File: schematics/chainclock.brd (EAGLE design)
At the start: 55 x 46.5 mm, 21 parts, among them SW1 ROTARTY_ENCODER

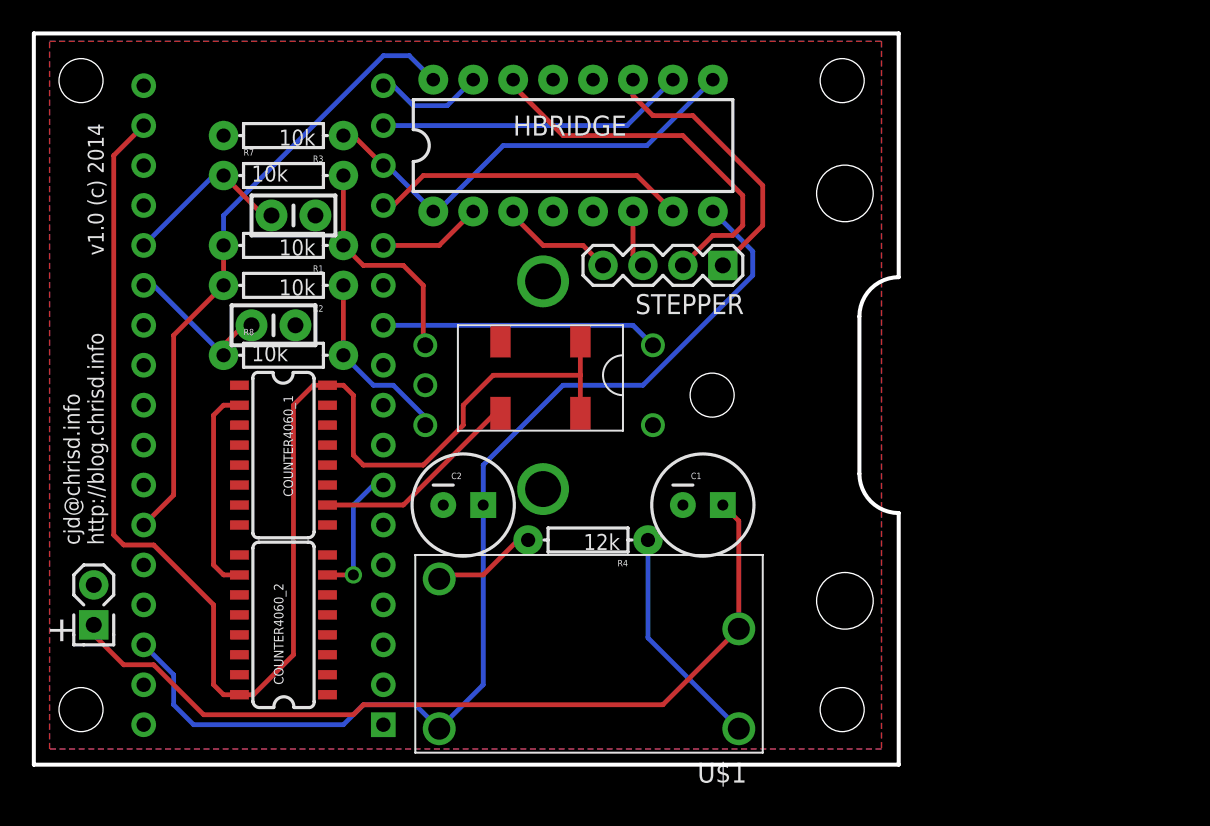
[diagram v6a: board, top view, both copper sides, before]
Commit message: Move power header
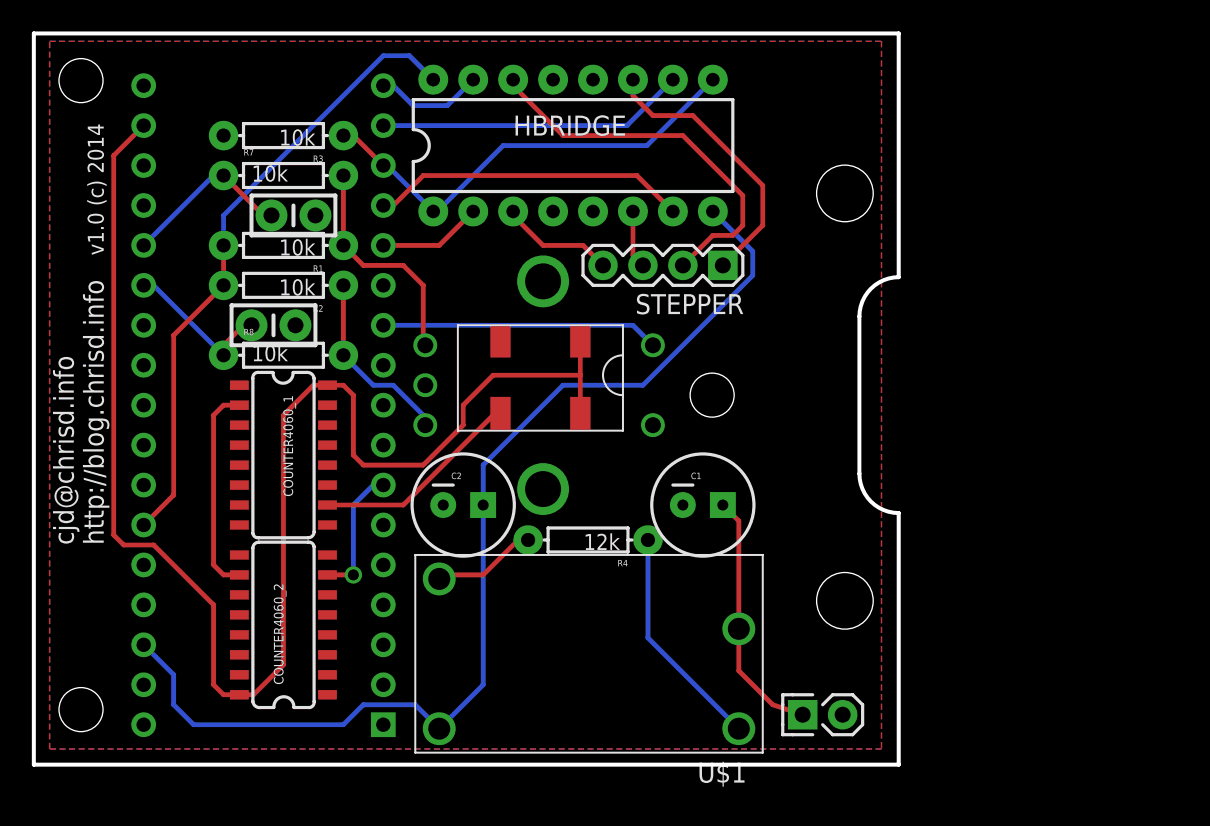
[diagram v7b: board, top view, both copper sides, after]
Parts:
- moved JP1 45.4 mm to (48.9, 3.17), turned to 0 degrees
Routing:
- net VBATT: track 54.3 -> 16.0 mm
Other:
- board text removed: "+"
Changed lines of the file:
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@@
 <hole x="3" y="43.5" drill="2.8"/>
 <hole x="43.135" y="23.5" drill="2.8"/>
-<text x="4.445" y="13.97" size="1.016" layer="21" rot="R90">cjd@chrisd.info
+<text x="4.445" y="13.97" size="1.27" layer="21" rot="R90">cjd@chrisd.info
 http://blog.chrisd.info</text>
-<hole x="51.405" y="3.5" drill="2.8"/>
-<hole x="51.405" y="43.5" drill="2.8"/>
 <wire x1="0" y1="0" x2="0" y2="46.5" width="0.254" layer="20"/>
 <wire x1="0" y1="46.5" x2="55" y2="46.5" width="0.254" layer="20"/>
@@
 <wire x1="55" y1="0" x2="0" y2="0" width="0.254" layer="20"/>
 <text x="4.445" y="32.385" size="1.016" layer="21" rot="R90">v1.0 (c) 2014</text>
-<text x="2.54" y="7.62" size="1.778" layer="21" rot="R90">+</text>
 </plain>
 <attributes>
@@
 <element name="C2" library="SparkFun-Capacitors" package="CPOL-RADIAL-100UF-25V" value="" x="27.305" y="16.51"/>
 <element name="R4" library="SparkFun-Resistors" package="AXIAL-0.3EZ" value="12k" x="35.2425" y="14.2875" rot="R180"/>
-<element name="JP1" library="desjardins" package="MOLEX-1X2" value="M02POLAR" x="3.81" y="8.89" rot="R90"/>
+<element name="JP1" library="desjardins" package="MOLEX-1X2" value="M02POLAR" x="48.895" y="3.175"/>
 <element name="COUNTER4060_1" library="desjardins" package="SO016" value="4060SOIC16" x="15.875" y="19.685" rot="R270"/>
 <element name="COUNTER4060_2" library="desjardins" package="SO016" value="4060SOIC16" x="15.875" y="8.89" rot="R90"/>
@@
 <wire x1="12.065" y1="4.445" x2="13.075" y2="4.445" width="0.3048" layer="1"/>
 <wire x1="18.675" y1="24.13" x2="17.78" y2="24.13" width="0.3048" layer="1"/>
-<wire x1="17.78" y1="24.13" x2="16.51" y2="22.86" width="0.3048" layer="1"/>
-<wire x1="16.51" y1="22.86" x2="16.51" y2="6.985" width="0.3048" layer="1"/>
-<wire x1="16.51" y1="6.985" x2="13.97" y2="4.445" width="0.3048" layer="1"/>
+<wire x1="17.78" y1="24.13" x2="15.875" y2="22.225" width="0.3048" layer="1"/>
+<wire x1="15.875" y1="22.225" x2="15.875" y2="6.35" width="0.3048" layer="1"/>
+<wire x1="15.875" y1="6.35" x2="13.97" y2="4.445" width="0.3048" layer="1"/>
 <wire x1="13.97" y1="4.445" x2="13.075" y2="4.445" width="0.3048" layer="1"/>
 </signal>
@@
 <contactref element="C1" pad="1"/>
 <contactref element="JP1" pad="1"/>
-<wire x1="3.81" y1="8.89" x2="3.81" y2="8.255" width="0.3048" layer="1"/>
-<wire x1="3.81" y1="8.255" x2="5.715" y2="6.35" width="0.3048" layer="1"/>
-<wire x1="5.715" y1="6.35" x2="7.62" y2="6.35" width="0.3048" layer="1"/>
-<wire x1="7.62" y1="6.35" x2="10.795" y2="3.175" width="0.3048" layer="1"/>
-<wire x1="10.795" y1="3.175" x2="20.32" y2="3.175" width="0.3048" layer="1"/>
-<wire x1="20.32" y1="3.175" x2="20.955" y2="3.81" width="0.3048" layer="1"/>
-<wire x1="20.955" y1="3.81" x2="40.005" y2="3.81" width="0.3048" layer="1"/>
-<wire x1="40.005" y1="3.81" x2="44.831" y2="8.636" width="0.3048" layer="1"/>
 <wire x1="44.831" y1="8.636" x2="44.831" y2="15.494" width="0.3048" layer="1"/>
 <wire x1="44.831" y1="15.494" x2="43.815" y2="16.51" width="0.3048" layer="1"/>
+<wire x1="44.831" y1="8.636" x2="44.831" y2="5.969" width="0.3048" layer="1"/>
+<wire x1="44.831" y1="5.969" x2="46.99" y2="3.81" width="0.3048" layer="1"/>
+<wire x1="46.99" y1="3.81" x2="48.895" y2="3.175" width="0.3048" layer="1"/>
 </signal>
 <signal name="Q13">

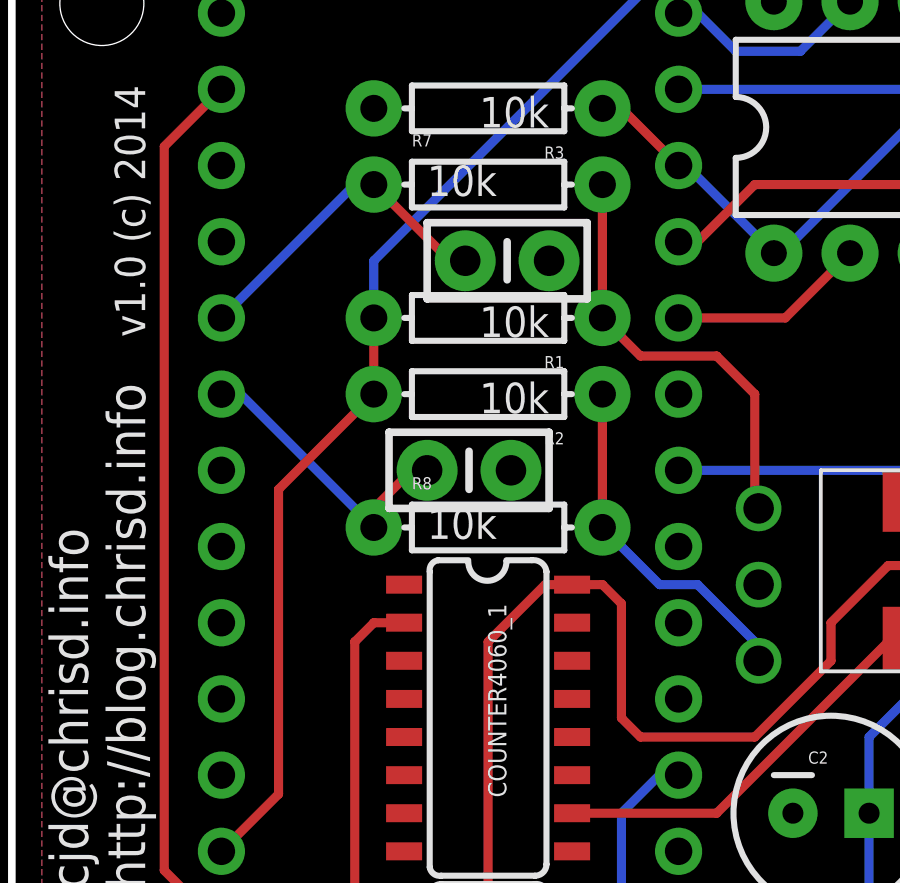
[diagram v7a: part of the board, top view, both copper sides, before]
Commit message: Use int line for rot enc
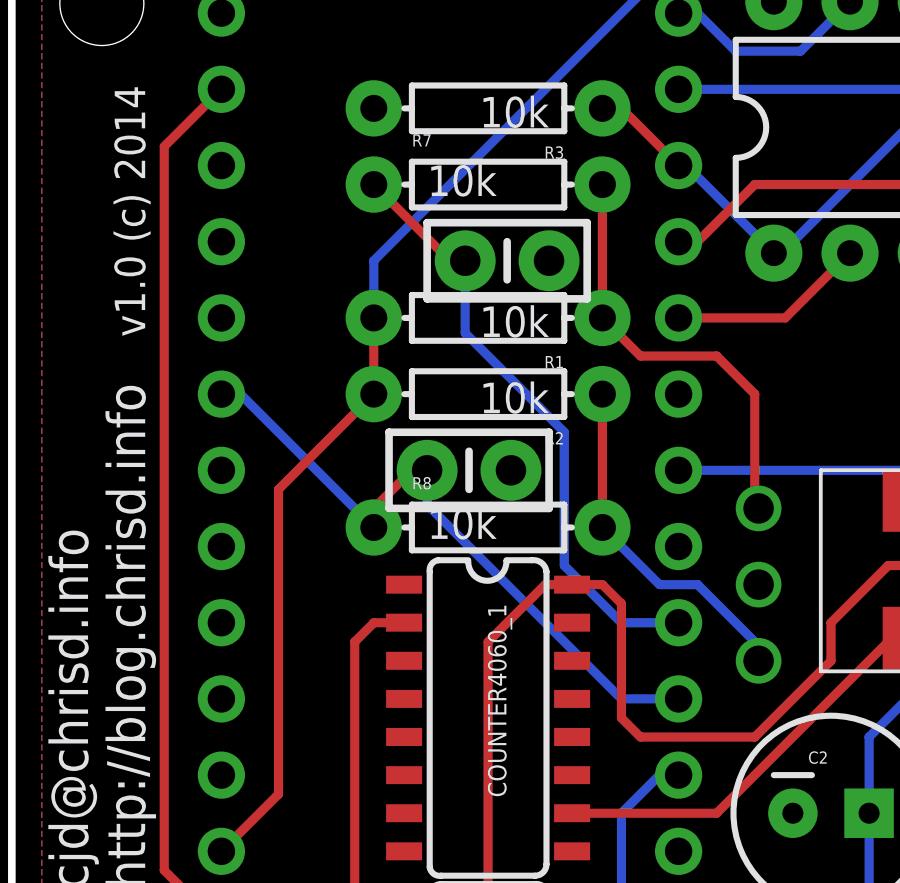
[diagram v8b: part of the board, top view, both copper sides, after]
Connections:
- net RENCA: now also U$4.P8; no longer U$4.P23
- net RENCB: now also U$4.P9; no longer U$4.P22
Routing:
- net RENCA: track 9.86 -> 21.4 mm
- net RENCB: track 11.0 -> 20.9 mm
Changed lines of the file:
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@@
 <grid distance="0.025" unitdist="inch" unit="inch" style="lines" multiple="1" display="yes" altdistance="0.025" altunitdist="inch" altunit="inch"/>
 <layers>
-<layer number="1" name="Top" color="4" fill="1" visible="yes" active="yes"/>
+<layer number="1" name="Top" color="4" fill="1" visible="no" active="yes"/>
 <layer number="16" name="Bottom" color="1" fill="1" visible="yes" active="yes"/>
 <layer number="17" name="Pads" color="2" fill="1" visible="yes" active="yes"/>
@@
 <contactref element="C6" pad="1"/>
 <contactref element="R7" pad="P$1"/>
-<contactref element="U$4" pad="P22"/>
-<wire x1="6.985" y1="33.02" x2="11.43" y2="37.465" width="0.3048" layer="16"/>
 <wire x1="11.43" y1="37.465" x2="12.065" y2="37.465" width="0.3048" layer="16"/>
 <wire x1="15.113" y1="34.925" x2="14.605" y2="34.925" width="0.3048" layer="1"/>
 <wire x1="14.605" y1="34.925" x2="12.065" y2="37.465" width="0.3048" layer="1"/>
+<contactref element="U$4" pad="P9"/>
+<wire x1="15.113" y1="34.925" x2="15.113" y2="32.512" width="0.3048" layer="16"/>
+<wire x1="15.113" y1="32.512" x2="18.415" y2="29.21" width="0.3048" layer="16"/>
+<wire x1="18.415" y1="29.21" x2="18.415" y2="24.765" width="0.3048" layer="16"/>
+<wire x1="18.415" y1="24.765" x2="20.32" y2="22.86" width="0.3048" layer="16"/>
+<wire x1="20.32" y1="22.86" x2="22.225" y2="22.86" width="0.3048" layer="16"/>
 </signal>
 <signal name="RENCA">
 <contactref element="C5" pad="1"/>
 <contactref element="R8" pad="P$1"/>
-<contactref element="U$4" pad="P23"/>
-<wire x1="6.985" y1="30.48" x2="7.62" y2="30.48" width="0.3048" layer="16"/>
 <wire x1="7.62" y1="30.48" x2="12.065" y2="26.035" width="0.3048" layer="16"/>
 <wire x1="12.065" y1="26.035" x2="12.065" y2="26.67" width="0.3048" layer="1"/>
 <wire x1="12.065" y1="26.67" x2="13.335" y2="27.94" width="0.3048" layer="1"/>
 <wire x1="13.335" y1="27.94" x2="13.843" y2="27.94" width="0.3048" layer="1"/>
+<contactref element="U$4" pad="P8"/>
+<wire x1="13.843" y1="27.94" x2="13.843" y2="26.797" width="0.3048" layer="16"/>
+<wire x1="13.843" y1="26.797" x2="20.32" y2="20.32" width="0.3048" layer="16"/>
+<wire x1="20.32" y1="20.32" x2="22.225" y2="20.32" width="0.3048" layer="16"/>
 </signal>
 <signal name="RTC">
